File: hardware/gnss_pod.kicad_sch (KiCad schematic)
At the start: 0 parts

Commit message: needs review
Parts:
- added J1: SQT-110-01-L-D, SQT11001LD, symbol gnsspod-sym:SQT-110-01-L-D
- added J2, J3: SSQ-126-04-G-D, RHDR52W64P254_2X26_6655X495X864P, symbol gnsspod-sym:SSQ-126-04-G-D
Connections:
- new net 3V3: J1.2 (3V3)
- new net GNDREF: J1.10 (GND), J1.13 (GND), J1.16 (GND), J1.18 (GND), J2.29, J2.30, J2.31, J2.32, J3.29, J3.30, J3.31, J3.32
- new net RX1: J1.12 (RXD1), J2.19
- new net TX1: J1.11 (TXD1), J2.17

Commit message: Updated layout + schematic
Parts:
- removed J2, J3: SSQ-126-04-G-D, RHDR52W64P254_2X26_6655X495X864P, symbol gnsspod-sym:SSQ-126-04-G-D
- added H1, H2, H3, H4, H5, H6, H7, H8: MountingHole, MountingHole:MountingHole_3mm_Pad, symbol Mechanical:MountingHole
- added J2, J3: SSQ-126-04-G-D, RHDR52W64P254_2X26_6655X495X864P, symbol SSQ-126-04-G-D:SSQ-126-04-G-D
- J1: footprint SQT11001LD -> gnss_pod_Bib:SQT11001LD
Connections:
- net GNDREF: now also J2.29, J2.30, J2.31, J2.32, J3.29, J3.30, J3.31, J3.32
- net RX1: now also J2.19
- net TX1: now also J2.17
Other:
- note added: "GNSS"
- note added: "Holder"
- note added: "Mounting Holes"
- company: (none) -> SpaceLab
- title: (none) -> GNSS POD - HOLDER

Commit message: Some changes, wip usb, layout wip
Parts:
- added J4, J5: Conn_01x02_Pin, symbol Connector:Conn_01x02_Pin
- added P1: USB_C_Plug_USB2.0, symbol Connector:USB_C_Plug_USB2.0
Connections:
- net GNDREF: now also P1.A1 (GND), P1.A12 (GND), P1.B1 (GND), P1.B12 (GND)
- net RX1: now also J4.2 (Pin_2)
- net TX1: now also J4.1 (Pin_1)
- net TX2: now reaches J1.14 (TXD2)
- net TX2: now also J5.1 (Pin_1)
- net RX2: now reaches J1.15 (RXD2)
- net RX2: now also J5.2 (Pin_2)
- net USB_N: now reaches J1.3 (USB-D)
- net USB_N: now also P1.A7 (D-)
- net USB_P: now reaches J1.4 (USB+D+/RXD3)
- net USB_P: now also P1.A6 (D+)
- new net: P1.A4 (VBUS), P1.A9 (VBUS), P1.B4 (VBUS), P1.B9 (VBUS)
- no-connect marks 0 -> 5
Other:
- note added: "<- REVISAR!"
- moved on the sheet: J1, J2, J3

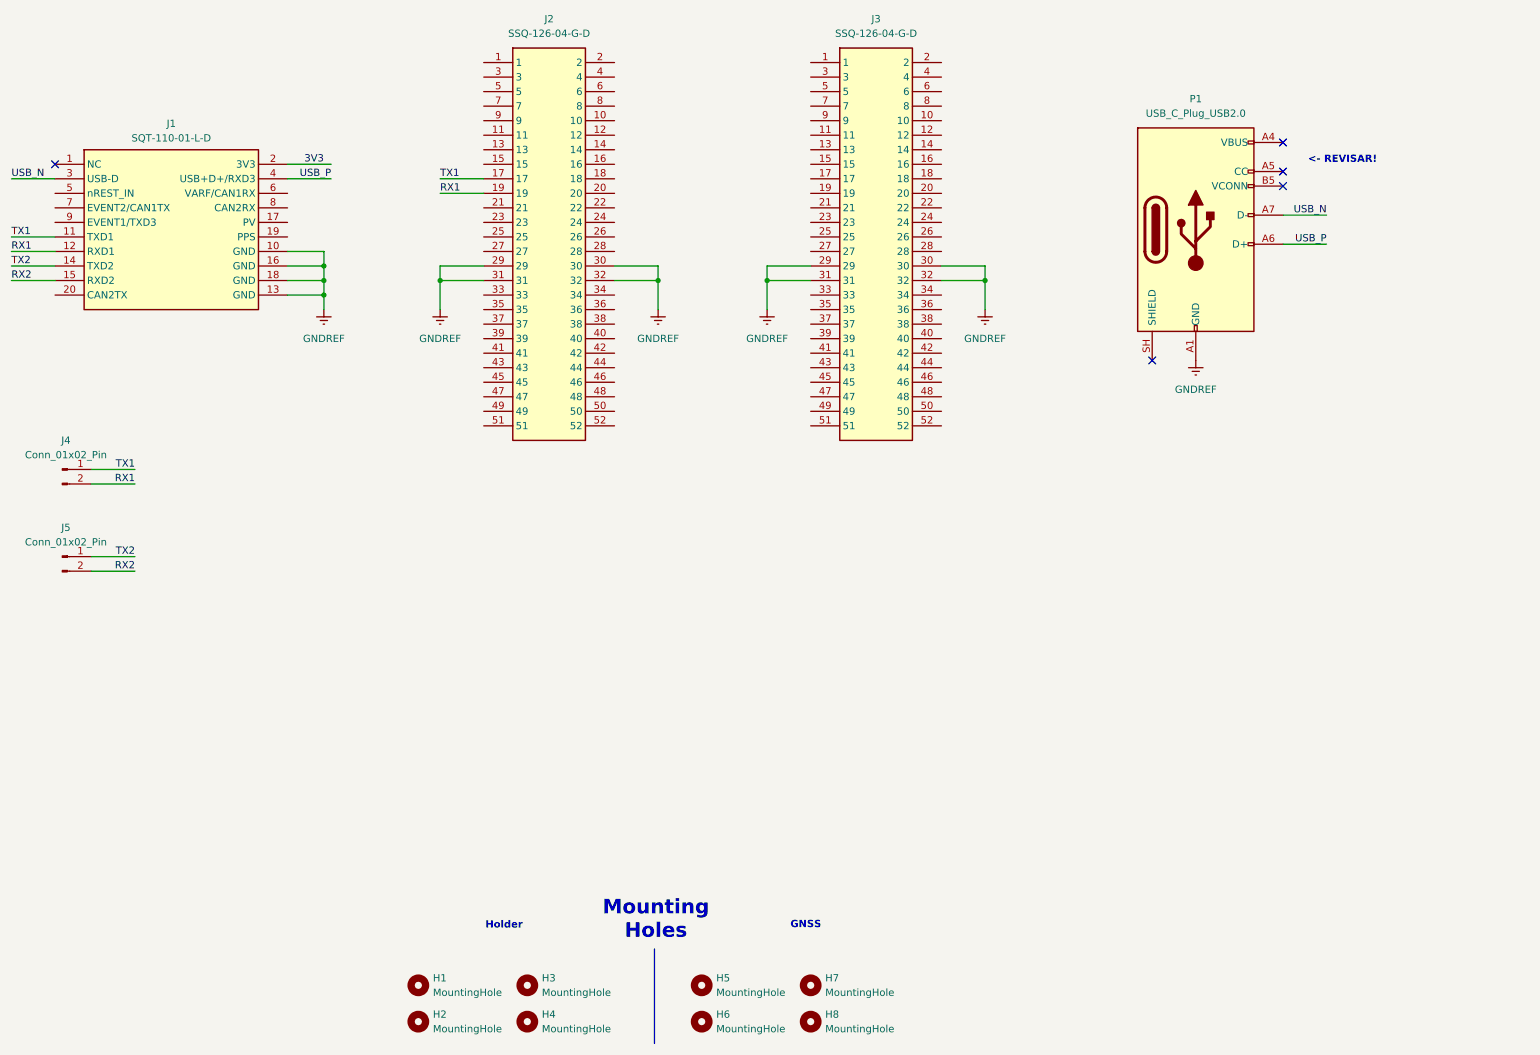
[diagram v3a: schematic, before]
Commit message: Layout modified according to INEP requirements
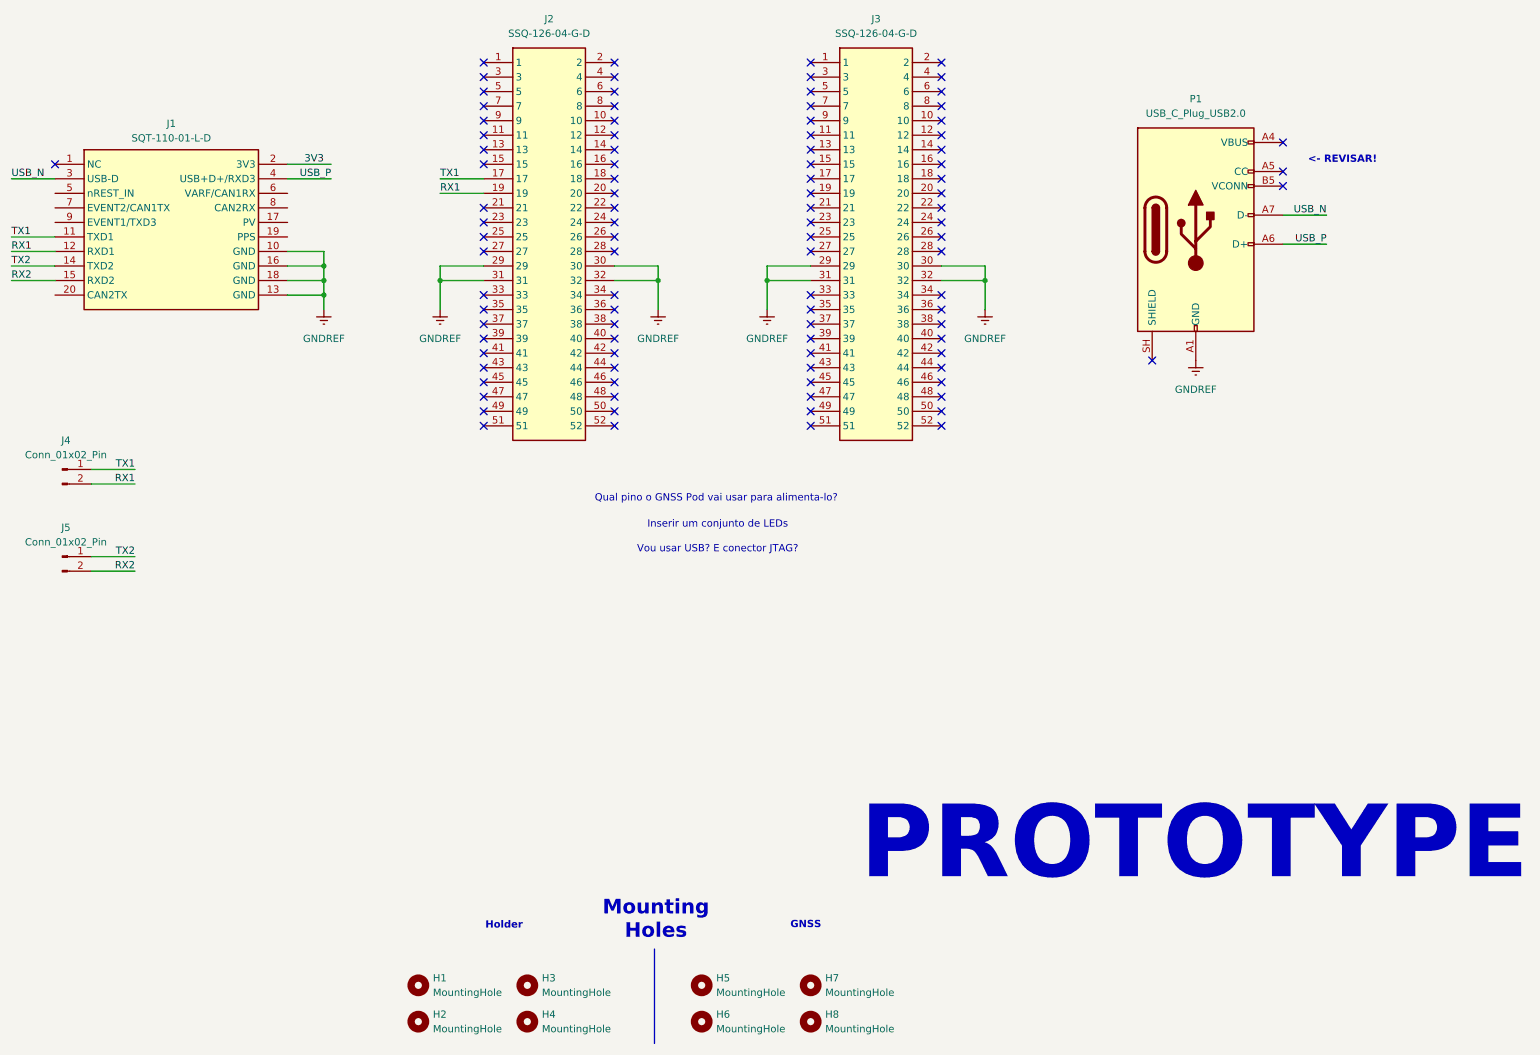
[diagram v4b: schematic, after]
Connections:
- no-connect marks 5 -> 99
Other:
- note added: "Inserir um conjunto de LEDs"
- note added: "PROTOTYPE"
- note added: "Qual pino o GNSS Pod vai usar para alimenta-lo?"
- note added: "Vou usar USB? E conector JTAG?"
